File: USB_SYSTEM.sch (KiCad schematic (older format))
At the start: 7 parts, among them J3 USB_B

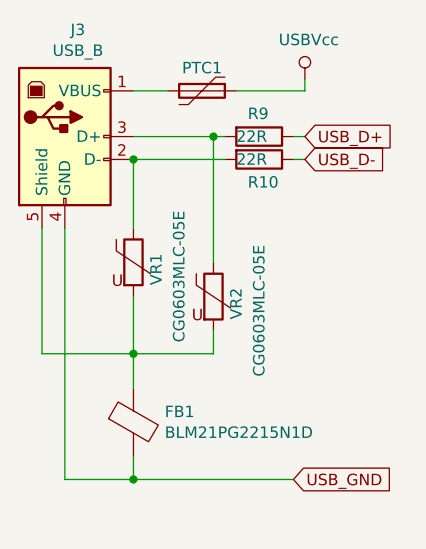
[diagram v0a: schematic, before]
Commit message: Set component footprints, added datasheets, fixed the last DRC error and a couple component values
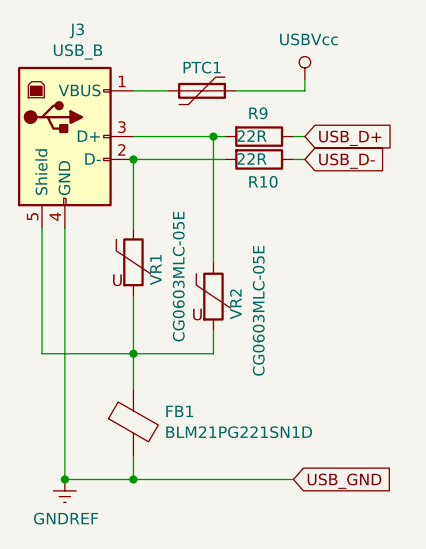
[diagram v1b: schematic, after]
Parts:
- FB1: value BLM21PG2215N1D -> BLM21PG221SN1D; footprint (none) -> Capacitor_SMD:C_0805_2012Metric
- J3: footprint (none) -> Connector_USB:USB_B_OST_USB-B1HSxx_Horizontal
- PTC1: footprint (none) -> Fuse:Fuse_1812_4532Metric
- R10, R9: footprint (none) -> Resistor_SMD:R_0603_1608Metric
- VR1, VR2: footprint (none) -> Capacitor_SMD:C_0603_1608Metric
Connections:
- net USB_GND renamed GNDREF
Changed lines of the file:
@@
 F 0 "J3" H 5457 3867 50  0000 C CNN
 F 1 "USB_B" H 5457 3776 50  0000 C CNN
-F 2 "" H 5550 3350 50  0001 C CNN
-F 3 " ~" H 5550 3350 50  0001 C CNN
+F 2 "Connector_USB:USB_B_OST_USB-B1HSxx_Horizontal" H 5550 3350 50  0001 C CNN
+F 3 "http://www.farnell.com/datasheets/2626186.pdf" H 5550 3350 50  0001 C CNN
 	1    5400 3400
 	1    0    0    -1
@@
 F 0 "R9" V 6150 3350 50  0000 L CNN
 F 1 "22R" V 6250 3300 50  0000 L CNN
-F 2 "" V 6180 3400 50  0001 C CNN
+F 2 "Resistor_SMD:R_0603_1608Metric" V 6180 3400 50  0001 C CNN
 F 3 "~" H 6250 3400 50  0001 C CNN
 	1    6250 3400
@@
 F 0 "R10" V 6350 3450 50  0000 L CNN
 F 1 "22R" V 6250 3400 50  0000 L CNN
-F 2 "" V 6180 3500 50  0001 C CNN
+F 2 "Resistor_SMD:R_0603_1608Metric" V 6180 3500 50  0001 C CNN
 F 3 "~" H 6250 3500 50  0001 C CNN
 	1    6250 3500
@@
 F 0 "PTC1" V 5900 3200 50  0000 C CNN
 F 1 "MF-MSMF-050-2" V 5866 3200 50  0001 C CNN
-F 2 "" H 6050 3000 50  0001 L CNN
-F 3 "~" H 6000 3200 50  0001 C CNN
+F 2 "Fuse:Fuse_1812_4532Metric" H 6050 3000 50  0001 L CNN
+F 3 "http://www.farnell.com/datasheets/2264697.pdf" H 6000 3200 50  0001 C CNN
 	1    6000 3200
 	0    1    1    0
@@
 F 0 "VR1" V 5800 3850 50  0000 L CNN
 F 1 "CG0603MLC-05E" V 5900 3600 50  0000 L CNN
-F 2 "" V 5630 3950 50  0001 C CNN
-F 3 "~" H 5700 3950 50  0001 C CNN
+F 2 "Capacitor_SMD:C_0603_1608Metric" V 5630 3950 50  0001 C CNN
+F 3 "http://www.farnell.com/datasheets/2360367.pdf" H 5700 3950 50  0001 C CNN
 	1    5700 3950
 	1    0    0    -1
@@
 F 0 "VR2" V 6150 4000 50  0000 L CNN
 F 1 "CG0603MLC-05E" V 6250 3750 50  0000 L CNN
-F 2 "" V 5980 4100 50  0001 C CNN
-F 3 "~" H 6050 4100 50  0001 C CNN
+F 2 "Capacitor_SMD:C_0603_1608Metric" V 5980 4100 50  0001 C CNN
+F 3 "http://www.farnell.com/datasheets/2360367.pdf" H 6050 4100 50  0001 C CNN
 	1    6050 4100
 	1    0    0    -1
@@
 AR Path="/5EC7AD45/5EC7D91B" Ref="FB1"  Part="1"
 F 0 "FB1" H 5837 4696 50  0000 L CNN
-F 1 "BLM21PG2215N1D" H 5837 4605 50  0000 L CNN
-F 2 "" V 5630 4650 50  0001 C CNN
-F 3 "~" H 5700 4650 50  0001 C CNN
+F 1 "BLM21PG221SN1D" H 5837 4605 50  0000 L CNN
+F 2 "Capacitor_SMD:C_0805_2012Metric" V 5630 4650 50  0001 C CNN
+F 3 "http://www.farnell.com/datasheets/1914683.pdf" H 5700 4650 50  0001 C CNN
 	1    5700 4650
 	1    0    0    -1
@@
 Wire Wire Line
 	5400 3800 5400 4900
+$Comp
+L power:GNDREF #PWR025
+U 1 1 5EC456E5
+P 5400 4900
+F 0 "#PWR025" H 5400 4650 50  0001 C CNN
+F 1 "GNDREF" H 5405 4727 50  0000 C CNN
+F 2 "" H 5400 4900 50  0001 C CNN
+F 3 "" H 5400 4900 50  0001 C CNN
+	1    5400 4900
+	1    0    0    -1
+$EndComp
+Connection ~ 5400 4900
 $EndSCHEMATC

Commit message: Updated the schematic, added missing footprints, started PCB design
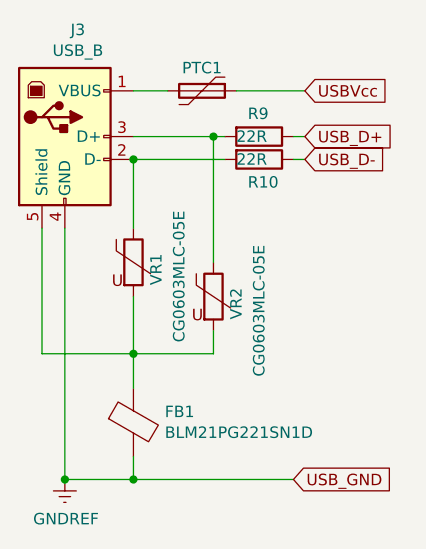
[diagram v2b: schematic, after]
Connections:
- net USBVcc: now reaches PTC1.1
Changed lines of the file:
@@
-	1    0    0    -1
-$EndComp
-$Comp
-L power_symbols:USBVcc #PWR?
-U 1 1 5EC7D8EB
-P 6450 3150
-AR Path="/5EC7D8EB" Ref="#PWR?"  Part="1"
-AR Path="/5EC7AD45/5EC7D8EB" Ref="#PWR024"  Part="1"
-F 0 "#PWR024" H 6450 3000 50  0001 C CNN
-F 1 "USBVcc" H 6467 3323 50  0000 C CNN
-F 2 "" H 6450 3150 50  0001 C CNN
-F 3 "" H 6450 3150 50  0001 C CNN
-	1    6450 3150
 	1    0    0    -1
 $EndComp
 Wire Wire Line
 	6150 3200 6450 3200
-Wire Wire Line
-	6450 3200 6450 3150
 Wire Wire Line
 	5700 3400 6050 3400
@@
 $EndComp
 Connection ~ 5400 4900
+Text GLabel 6450 3200 2    50   Input ~ 0
+USBVcc
 $EndSCHEMATC
